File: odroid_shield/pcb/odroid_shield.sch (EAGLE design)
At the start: 7 parts, among them J4 ODROID_J4

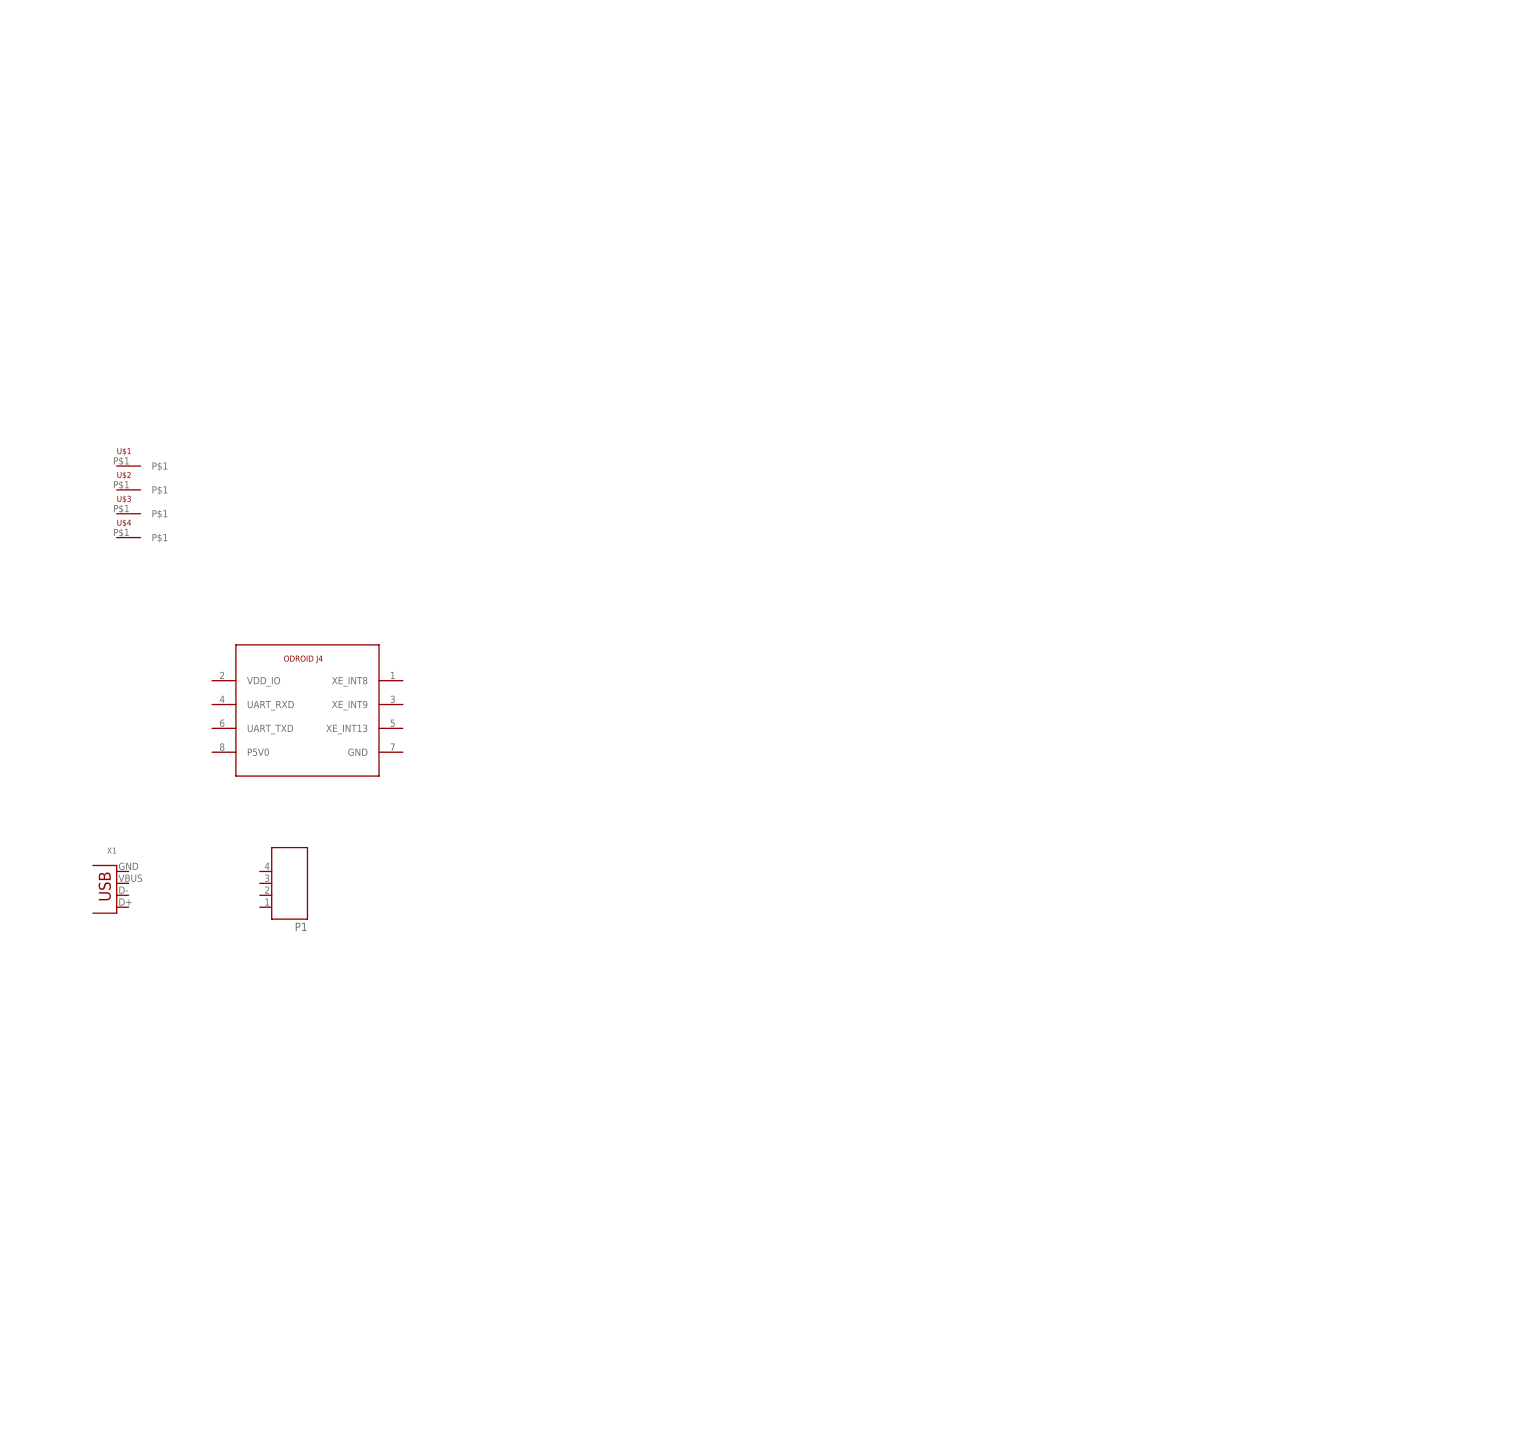
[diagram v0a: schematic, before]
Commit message: Progress on odroid shield.
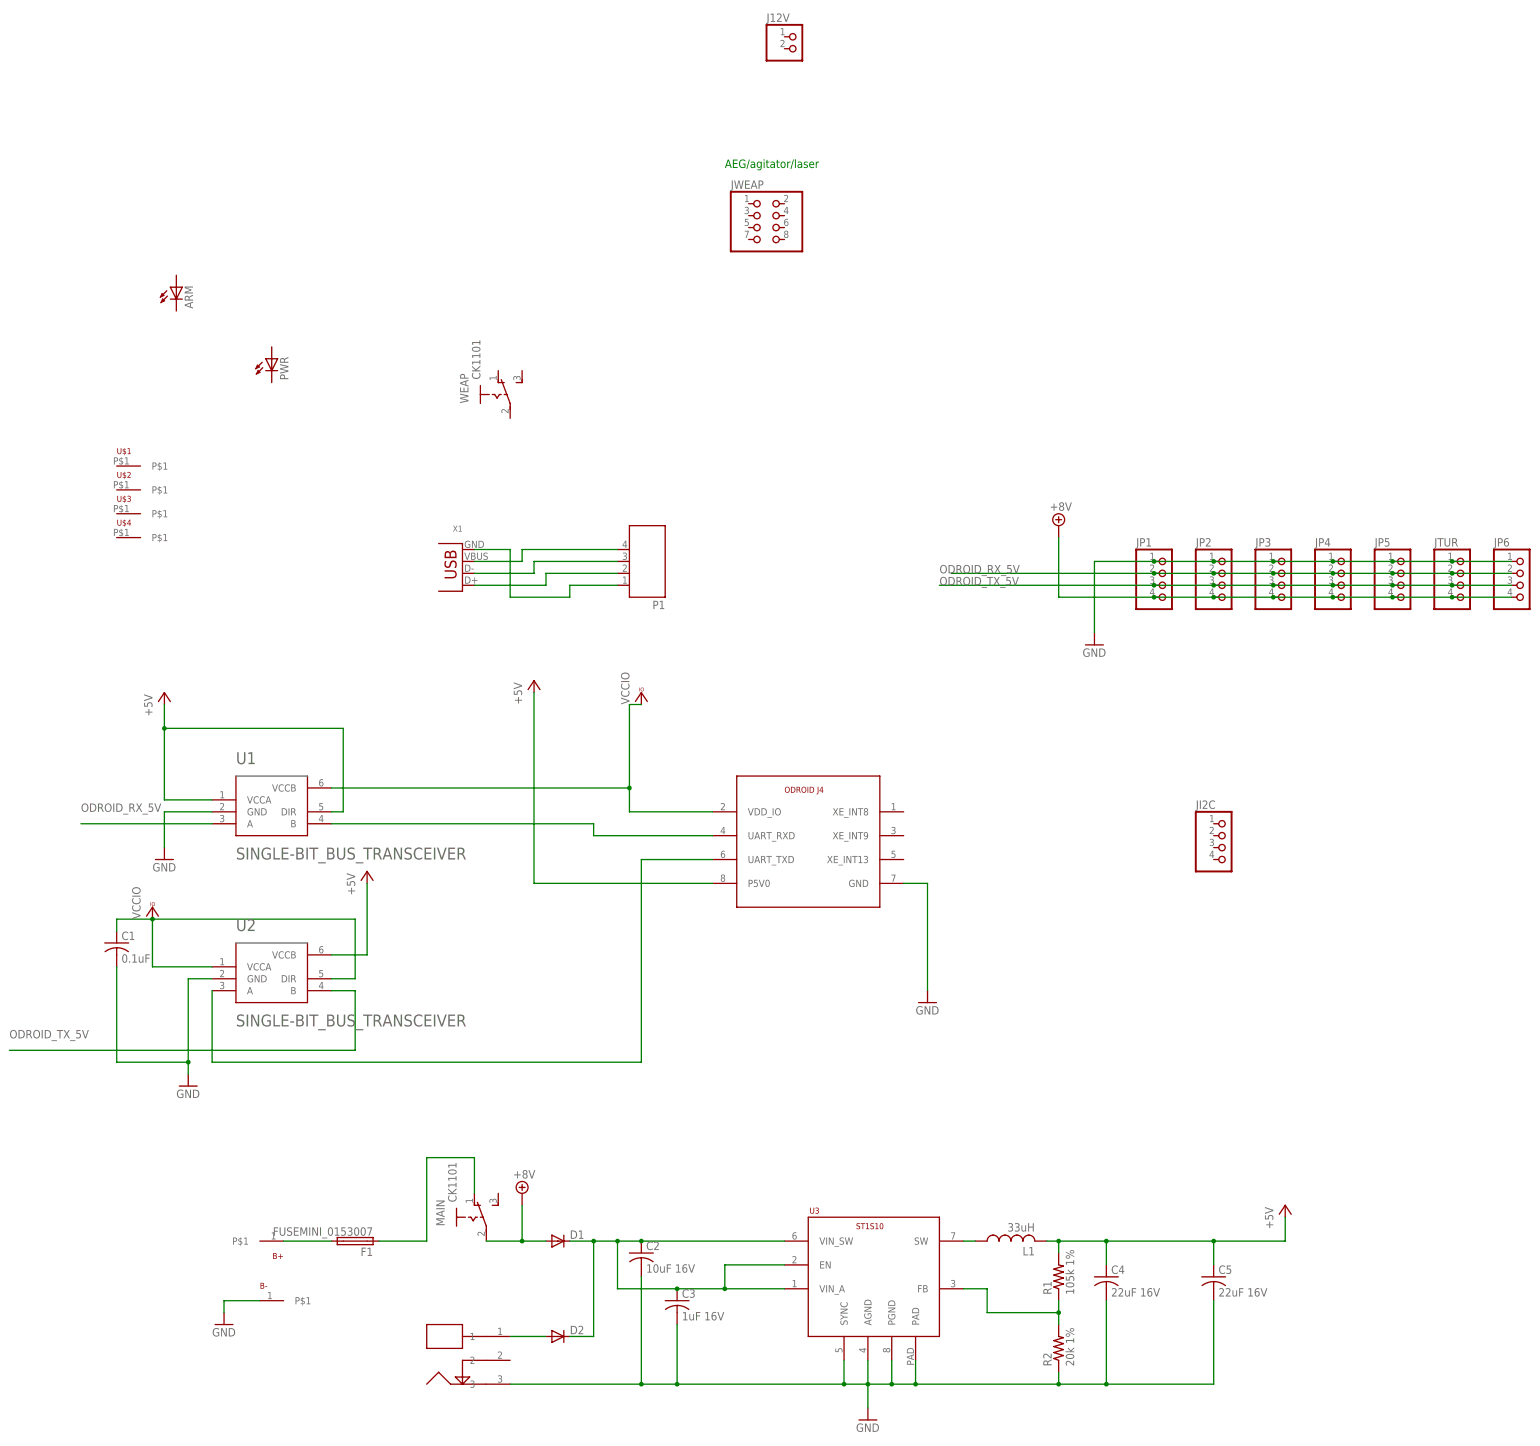
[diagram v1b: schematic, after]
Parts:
- added ARM: (no value), led:LED5MM
- added B+, B-: BAT_TERM, odroid_shield:BAT_TERM
- added C1: 0.1uF, rcl:C-USC0603
- added C2: 10uF 16V, rcl:C-USC1206
- added C3: 1uF 16V, rcl:C-USC0603
- added C4, C5: 22uF 16V, rcl:C-USC1206
- added D1, D2: (no value), odroid_shield:DIODE-CMS06
- added F1: FUSEMINI_0153007, odroid_shield:FUSEMINI_0153007
- added J12V: (no value), pinhead:PINHD-1X2
- added JI2C, JP1, JP2, JP3, JP4, JP5, JP6, JTUR: (no value), pinhead:PINHD-1X4
- added JWEAP: (no value), pinhead:PINHD-2X4
- added L1: 33uH, odroid_shield:L-USWURTH_74404042033
- added MAIN, WEAP: CK1101, odroid_shield:CK1101
- added PWR: (no value), led:LEDCHIPLED_0805
- added R1: 105k 1%, rcl:R-US_R0603
- added R2: 20k 1%, rcl:R-US_R0603
- added SHORE: PJ-034A, odroid_shield:PJ-034A
- added U1, U2: SINGLE-BIT_BUS_TRANSCEIVER, odroid_shield:SINGLE-BIT_BUS_TRANSCEIVER
- added U3: ST1S10, odroid_shield:ST1S10
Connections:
- new net +5V: C4.1, C5.1, J4.P5V0, L1.2, R1.2, U1.DIR, U1.VCCA, U2.VCCB
- new net +8V: D1.A, JP1.4, JP2.4, JP3.4, JP4.4, JP5.4, JP6.4, JTUR.4, MAIN.P
- new net GND: B-.P$1, C1.2, C2.2, C3.2, C4.2, C5.2, J4.GND, JP1.1, JP2.1, JP3.1, JP4.1, JP5.1, JP6.1, JTUR.1, R2.1, SHORE.3, U1.GND, U2.GND, U3.AGND, U3.PAD, U3.PGND, U3.SYNC
- new net N$1: P1.4, X1.VBUS
- new net N$10: L1.1, U3.SW
- new net N$11: C2.1, C3.1, D1.C, D2.C, U3.EN, U3.VIN_A, U3.VIN_SW
- new net N$13: R1.1, R2.2, U3.FB
- new net N$2: J4.UART_RXD, U1.B
- new net N$3: P1.3, X1.D-
- new net N$4: J4.UART_TXD, U2.A
- new net N$5: P1.2, X1.D+
- new net N$6: P1.1, X1.GND
- new net N$7: B+.P$1, F1.2
- new net N$8: F1.1, MAIN.O
- new net N$9: D2.A, SHORE.1
- new net ODROID_RX_5V: JP1.2, JP2.2, JP3.2, JP4.2, JP5.2, JP6.2, JTUR.2, U1.A
- new net ODROID_TX_5V: JP1.3, JP2.3, JP3.3, JP4.3, JP5.3, JP6.3, JTUR.3, U2.B
- new net VCCIO: C1.1, J4.VDD_IO, U1.VCCB, U2.DIR, U2.VCCA
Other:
- note added: "AEG/agitator/laser"
- moved on the sheet: P1, X1

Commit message: Continued work on odroid shield.
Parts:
- added C10, C9: 1uF, rcl:C-USC0603
- added C6, C7: .1uF, rcl:C-USC0603
- added C8: 10uF 16V, rcl:C-USC1206
- added IC1: TS5205, v-reg:TS5205
- added IND: (no value), led:LEDCHIPLED_0805
- added J1: AVRISP6_COMPACT, odroid_shield:AVRISP6_COMPACT
- added R10, R7, R8, R9: 4.7k, rcl:R-US_R0603
- added R11, R6: 200, rcl:R-US_R0603
- added R3, R4: 500, rcl:R-US_R0603
- added R5: 100k, rcl:R-US_R0603
- added SER2: (no value), pinhead:PINHD-1X4
- added T1: (no value), zetex:NMOSSOT23
- added U$5: MP33926, odroid_shield:MP33926
- added U$6: TCA9517MSOP8, odroid_shield:TCA9517MSOP8
- added U4: ATMEGA644P-20AU, odroid_shield:ATMEGA644P-20AU
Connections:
- new net +3V3: C9.1, IC1.VOUT, JWEAP.5
- new net AEG_PWM: U$5.IN1, U4.PD4
- new net AGITATOR_PWM: U$5.IN2, U4.PD5
- new net MOTOR_D1: U$5.D1, U4.PC2
- new net MOTOR_D2: U$5.D2/, U4.PC3
- new net MOTOR_EN: U$5.EN, U4.PC4
- new net MOTOR_FB: R6.2, U$5.FB, U4.PA0
- new net N$12: JWEAP.1, U$5.OUT1
- new net N$14: JWEAP.3, U$5.OUT2
- new net N$15: C6.1, C7.1, C8.1, R3.2, U$5.VPWR, WEAP.P
- new net N$16: C6.2, U$5.CCP
- new net N$17: R5.1, U$5.SF/
- new net N$18: IND.C
- new net N$19: JWEAP.6, T1.D
- new net N$20: ARM.A, R3.1
- new net N$21: J1.!RESET, U4.~RESET
- new net N$22: PWR.A, R4.1
- new net N$23: J1.SCK, U4.PB7
- new net N$24: J1.MOSI, U4.PB5
- new net N$25: J1.MISO, U4.PB6
- new net N$26: SER2.3, U4.PD3
- new net N$27: SER2.2, U4.PD2
- new net N$28: IND.A, R11.1
- new net N$29: R11.2, U4.PC5
- new net ODROID_SCL: J4.XE_INT8, R7.1, U$6.SCLA
- new net ODROID_SDA: J4.XE_INT9, R8.1, U$6.SDAA
- new net SYS_SCL: JI2C.3, R10.1, U$6.SCLB, U4.PC0
- new net SYS_SDA: JI2C.2, R9.1, U$6.SDAB, U4.PC1
- net +5V: now also C10.1, IC1.CE, IC1.VIN, J1.VCC, JI2C.1, R10.2, R5.2, R9.2, SER2.4, U$5.SLEW, U$6.EN, U$6.VCCB, U4.AVCC, U4.VCC, U4.VCC_2, U4.VCC_3
- net +8V: now also R4.2, WEAP.O
- net GND: now also ARM.C, C10.2, C7.2, C8.2, C9.2, IC1.GND, J1.GND, JI2C.4, JWEAP.2, JWEAP.4, PWR.C, R6.1, SER2.1, T1.S, U$5.AGND, U$5.PAD, U$5.PGND, U$6.GND, U4.GND, U4.GND_2, U4.GND_3, U4.GND_4
- net ODROID_RX_5V: now also U4.PD1
- net ODROID_TX_5V: now also U4.PD0
- net VCCIO: now also R7.2, R8.2, U$6.VCCA
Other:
- moved on the sheet: ARM, B+, B-, F1, J12V, JI2C, JWEAP, MAIN, PWR, WEAP

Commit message: Further progress on odroid shield.
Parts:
- removed J12V: (no value), pinhead:PINHD-1X2
- removed JP1, JP2, JP3, JP4, JP5, JP6, JTUR: (no value), pinhead:PINHD-1X4
- added C11, C12: 20pF, rcl:C-USC0603
- added JD1, JD2, JD3, JD4, JD5: JST-XH4SMT_RA, odroid_shield:JST-XH4SMT_RA
- added JD6, JD7: JST-XH4VERT, odroid_shield:JST-XH4VERT
- added R12: 100k, rcl:R-US_R0603
- added U$7: ABM8G, odroid_shield:ABM8G
- added U$8: MAX21000, odroid_shield:MAX21000
- F1: value FUSEMINI_0153007 -> FUSE; device odroid_shield:FUSEMINI_0153007 -> odroid_shield:FUSE; DPN F064-ND -> 36-3569-ND
- SHORE: value PJ-034A -> PJ-034ASMT; device odroid_shield:PJ-034A -> odroid_shield:PJ-034ASMT; DPN (none) -> CP-015AHPJ-CT-ND
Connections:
- new net N$32: C12.1, U$7.OSC@1, U4.XTAL2
- new net N$33: C11.1, U$7.OSC@3, U4.XTAL1
- net +3V3: now also JI2C.1, R10.2, R12.2, R9.2, U$6.EN, U$6.VCCB, U$8.VDD, U$8.VDDIO
- net +5V: no longer JI2C.1, R10.2, R9.2, U$6.EN, U$6.VCCB
- net +8V: now also JD1.4, JD2.4, JD3.4, JD4.4, JD5.4, JD6.4, JD7.4; no longer JP1.4, JP2.4, JP3.4, JP4.4, JP5.4, JP6.4, JTUR.4
- net GND: now also C11.2, C12.2, IND.C, JD1.1, JD2.1, JD3.1, JD4.1, JD5.1, JD6.1, JD7.1, U$7.GND@2, U$7.GND@4, U$8.CS, U$8.GND; no longer JP1.1, JP2.1, JP3.1, JP4.1, JP5.1, JP6.1, JTUR.1
- net N$18: now also R12.1, U$8.SA0; no longer IND.C
- net ODROID_RX_5V: now also JD1.2, JD2.2, JD3.2, JD4.2, JD5.2, JD6.2, JD7.2; no longer JP1.2, JP2.2, JP3.2, JP4.2, JP5.2, JP6.2, JTUR.2
- net ODROID_TX_5V: now also JD1.3, JD2.3, JD3.3, JD4.3, JD5.3, JD6.3, JD7.3; no longer JP1.3, JP2.3, JP3.3, JP4.3, JP5.3, JP6.3, JTUR.3
- net SYS_SCL: now also U$8.SCL
- net SYS_SDA: now also U$8.SDA

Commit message: odroid_shield: Complete rough draft of schematic.
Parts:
- added C13, C14, C15: .1uF, rcl:C-USC0603
- added U$9: MMA8451Q, odroid_shield:MMA8451Q
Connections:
- new net N$36: C15.1, U$9.BYP
- net +3V3: now also C13.1, C14.1, U$9.SA0, U$9.VDD, U$9.VDDIO
- net GND: now also C13.2, C14.2, C15.2, U$9.GND
- net SYS_SCL: now also U$9.SCL
- net SYS_SDA: now also U$9.SDA
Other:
- moved on the sheet: U3
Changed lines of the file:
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@@
 <part name="+3V4" library="supply1" deviceset="+3V3" device=""/>
 <part name="R12" library="rcl" deviceset="R-US_" device="R0603" value="100k"/>
+<part name="C13" library="rcl" deviceset="C-US" device="C0603" value=".1uF"/>
+<part name="U$9" library="odroid_shield" deviceset="MMA8451Q" device=""/>
+<part name="+3V5" library="supply1" deviceset="+3V3" device=""/>
+<part name="GND16" library="supply1" deviceset="GND" device=""/>
+<part name="C14" library="rcl" deviceset="C-US" device="C0603" value=".1uF"/>
+<part name="C15" library="rcl" deviceset="C-US" device="C0603" value=".1uF"/>
 </parts>
 <sheets>
@@
 <instance part="+3V4" gate="G$1" x="48.26" y="447.04"/>
 <instance part="R12" gate="G$1" x="96.52" y="426.72" rot="R90"/>
+<instance part="C13" gate="G$1" x="35.56" y="411.48"/>
+<instance part="U$9" gate="G$1" x="182.88" y="403.86"/>
+<instance part="+3V5" gate="G$1" x="137.16" y="439.42"/>
+<instance part="GND16" gate="1" x="182.88" y="378.46"/>
+<instance part="C14" gate="G$1" x="142.24" y="393.7"/>
+<instance part="C15" gate="G$1" x="152.4" y="393.7"/>
 </instances>
 <busses>
@@
 <wire x1="91.44" y1="383.54" x2="73.66" y2="383.54" width="0.1524" layer="91"/>
 <junction x="73.66" y="383.54"/>
+<pinref part="C13" gate="G$1" pin="2"/>
+<wire x1="35.56" y1="406.4" x2="35.56" y2="383.54" width="0.1524" layer="91"/>
+<wire x1="35.56" y1="383.54" x2="55.88" y2="383.54" width="0.1524" layer="91"/>
+<junction x="55.88" y="383.54"/>
+</segment>
+<segment>
+<pinref part="U$9" gate="G$1" pin="GND"/>
+<wire x1="167.64" y1="393.7" x2="167.64" y2="381" width="0.1524" layer="91"/>
+<pinref part="GND16" gate="1" pin="GND"/>
+<wire x1="167.64" y1="381" x2="182.88" y2="381" width="0.1524" layer="91"/>
+<pinref part="C14" gate="G$1" pin="2"/>
+<wire x1="142.24" y1="388.62" x2="142.24" y2="381" width="0.1524" layer="91"/>
+<wire x1="142.24" y1="381" x2="152.4" y2="381" width="0.1524" layer="91"/>
+<junction x="167.64" y="381"/>
+<pinref part="C15" gate="G$1" pin="2"/>
+<wire x1="152.4" y1="381" x2="167.64" y2="381" width="0.1524" layer="91"/>
+<wire x1="152.4" y1="388.62" x2="152.4" y2="381" width="0.1524" layer="91"/>
+<junction x="152.4" y="381"/>
 </segment>
 </net>
@@
 <wire x1="96.52" y1="436.88" x2="96.52" y2="431.8" width="0.1524" layer="91"/>
 <junction x="48.26" y="436.88"/>
+<pinref part="C13" gate="G$1" pin="1"/>
+<wire x1="35.56" y1="414.02" x2="35.56" y2="416.56" width="0.1524" layer="91"/>
+<wire x1="35.56" y1="416.56" x2="48.26" y2="416.56" width="0.1524" layer="91"/>
+</segment>
+<segment>
+<pinref part="+3V5" gate="G$1" pin="+3V3"/>
+<wire x1="137.16" y1="436.88" x2="137.16" y2="426.72" width="0.1524" layer="91"/>
+<pinref part="U$9" gate="G$1" pin="VDD"/>
+<wire x1="137.16" y1="426.72" x2="137.16" y2="411.48" width="0.1524" layer="91"/>
+<wire x1="137.16" y1="411.48" x2="142.24" y2="411.48" width="0.1524" layer="91"/>
+<wire x1="142.24" y1="411.48" x2="167.64" y2="411.48" width="0.1524" layer="91"/>
+<wire x1="137.16" y1="411.48" x2="137.16" y2="401.32" width="0.1524" layer="91"/>
+<junction x="137.16" y="411.48"/>
+<pinref part="U$9" gate="G$1" pin="VDDIO"/>
+<wire x1="137.16" y1="401.32" x2="167.64" y2="401.32" width="0.1524" layer="91"/>
+<pinref part="C14" gate="G$1" pin="1"/>
+<wire x1="142.24" y1="396.24" x2="142.24" y2="411.48" width="0.1524" layer="91"/>
+<junction x="142.24" y="411.48"/>
+<pinref part="U$9" gate="G$1" pin="SA0"/>
+<wire x1="198.12" y1="403.86" x2="203.2" y2="403.86" width="0.1524" layer="91"/>
+<wire x1="203.2" y1="403.86" x2="203.2" y2="426.72" width="0.1524" layer="91"/>
+<wire x1="203.2" y1="426.72" x2="137.16" y2="426.72" width="0.1524" layer="91"/>
+<junction x="137.16" y="426.72"/>
 </segment>
 </net>
@@
 <label x="106.68" y="416.56" size="1.778" layer="95"/>
 </segment>
+<segment>
+<pinref part="U$9" gate="G$1" pin="SCL"/>
+<wire x1="198.12" y1="411.48" x2="228.6" y2="411.48" width="0.1524" layer="91"/>
+<label x="218.44" y="411.48" size="1.778" layer="95"/>
+</segment>
 </net>
 <net name="SYS_SDA" class="0">
@@
 <label x="106.68" y="414.02" size="1.778" layer="95"/>
 </segment>
+<segment>
+<pinref part="U$9" gate="G$1" pin="SDA"/>
+<wire x1="198.12" y1="408.94" x2="228.6" y2="408.94" width="0.1524" layer="91"/>
+<label x="218.44" y="408.94" size="1.778" layer="95"/>
+</segment>
 </net>
 <net name="N$21" class="0">
@@
 </segment>
 </net>
+<net name="N$36" class="0">
+<segment>
+<pinref part="C15" gate="G$1" pin="1"/>
+<wire x1="152.4" y1="396.24" x2="152.4" y2="406.4" width="0.1524" layer="91"/>
+<pinref part="U$9" gate="G$1" pin="BYP"/>
+<wire x1="152.4" y1="406.4" x2="167.64" y2="406.4" width="0.1524" layer="91"/>
+</segment>
+</net>

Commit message: odroid_shield: Fix some DPNs and move the 3.3V regulator to a slightly better spot.
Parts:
- JD6, JD7: DPN S9410-ND -> 455-2249-ND
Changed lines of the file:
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@@
 <part name="JWEAP" library="pinhead" deviceset="PINHD-2X4" device=""/>
 <part name="JD6" library="odroid_shield" deviceset="JST-XH4" device="VERT">
-<attribute name="DPN" value="S9410-ND"/>
+<attribute name="DPN" value="455-2249-ND"/>
 </part>
 <part name="B+" library="odroid_shield" deviceset="BAT_TERM" device=""/>
@@
 <part name="SUPPLY2" library="supply2" deviceset="+8V" device=""/>
 <part name="JD7" library="odroid_shield" deviceset="JST-XH4" device="VERT">
-<attribute name="DPN" value="S9410-ND"/>
+<attribute name="DPN" value="455-2249-ND"/>
 </part>
 <part name="GND7" library="supply1" deviceset="GND" device=""/>

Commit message: odroid_shield: Tried to name all parts.  Actually connected up the laser FET.
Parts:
- renumbered IC1 to U5, P1 to JUSB, T1 to Q1, U$5 to U7, U$6 to U6, U$7 to U10, U$8 to U8, U$9 to U9, X1 to J2
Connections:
- new net LASER_EN: Q1.G, U4.PC6
